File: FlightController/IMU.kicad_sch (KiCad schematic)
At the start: 9 parts, among them U4 ICM-42688-P, U5 BMP390

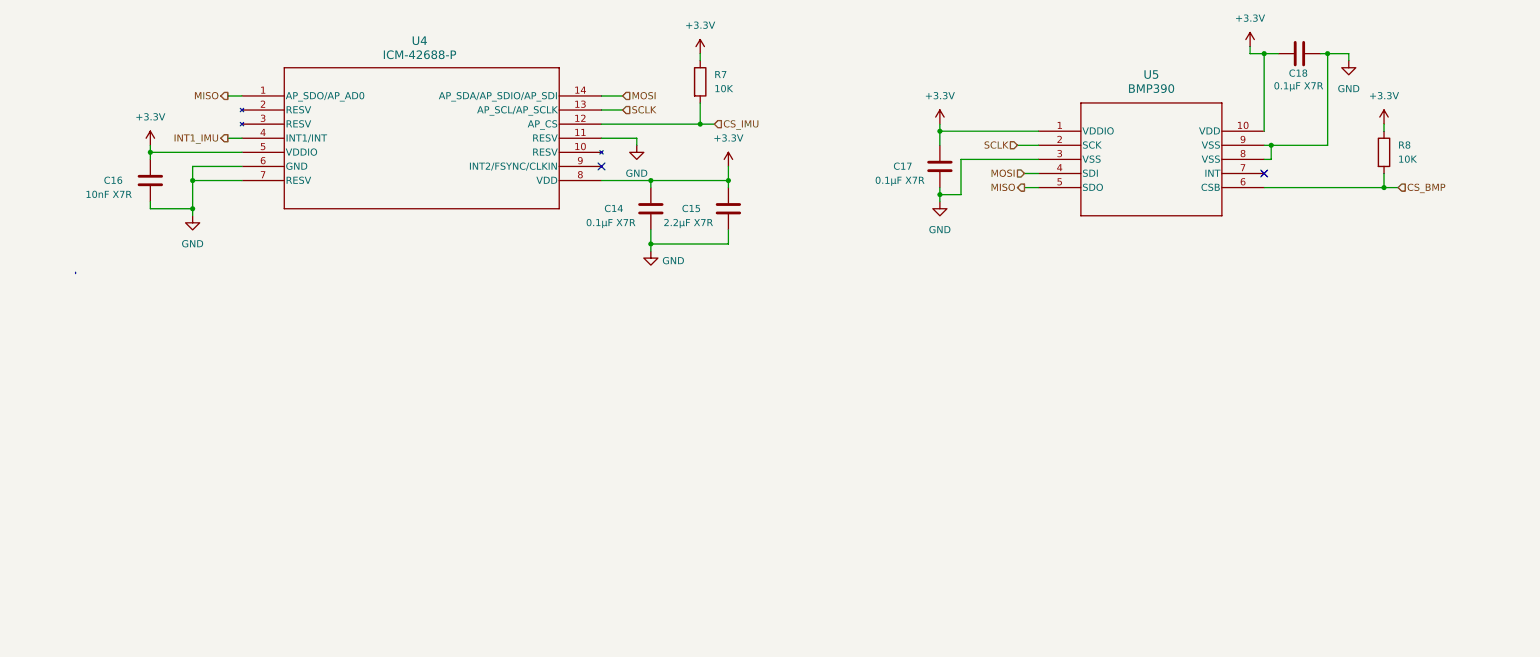
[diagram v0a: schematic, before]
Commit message: Added Part numbers and Buck in PCB
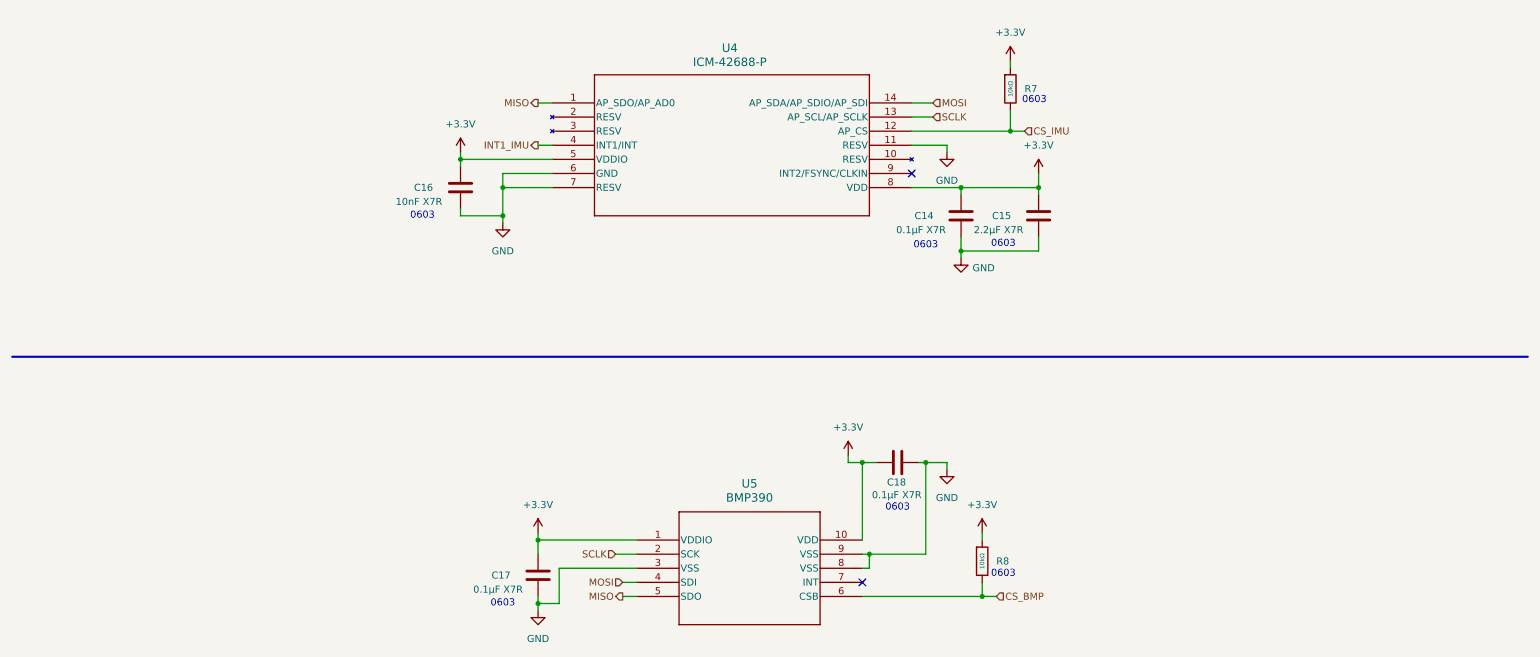
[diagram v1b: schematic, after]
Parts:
- removed R7, R8: 10K, Resistor_SMD:R_1206_3216Metric_Pad1.30x1.75mm_HandSolder, symbol Device:R
- added R7, R8: 10kΩ, PCM_JLCPCB:R_0603, symbol PCM_JLCPCB-Resistors:0603,10kΩ
- C14, C17, C18: footprint Capacitor_SMD:C_1206_3216Metric_Pad1.33x1.80mm_HandSolder -> Capacitor_SMD:C_0603_1608Metric_Pad1.08x0.95mm_HandSolder; LCSC (none) -> C1590
- C15: footprint Capacitor_SMD:C_1206_3216Metric_Pad1.33x1.80mm_HandSolder -> Capacitor_SMD:C_0603_1608Metric_Pad1.08x0.95mm_HandSolder; LCSC (none) -> C43922
- C16: footprint Capacitor_SMD:C_1206_3216Metric_Pad1.33x1.80mm_HandSolder -> Capacitor_SMD:C_0603_1608Metric_Pad1.08x0.95mm_HandSolder; LCSC (none) -> C1589
- U4, U5: now left out of the parts list
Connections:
- net +3.3V: now also R7.1, R8.1
- net CS_BMP: now also R8.2
- net CS_IMU: now also R7.2
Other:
- note added: "0603"
- moved on the sheet: C14, C15, C16, C17, C18, U4, U5
